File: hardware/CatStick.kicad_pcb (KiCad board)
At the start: 4 copper layers, 81 x 20 mm, 80 parts, among them J1 Antenna, J2 Conn_01x06_Female, J3 Conn_01x06_Female, P1 USB_C_Plug_USB2.0, SW1 SW, U1 AP2112K-3.3, U2 RFSW8006QTR7, U3 ATSAMD21E18A, U4 0900PC15A0036, U5 0900FM15D0039, U6 SW409, U7 SX1262IMLTRT, U8 CC1352R1F3RGZR, Y1 48MHz, Y2 32.768kHz, Y3 32Mhz

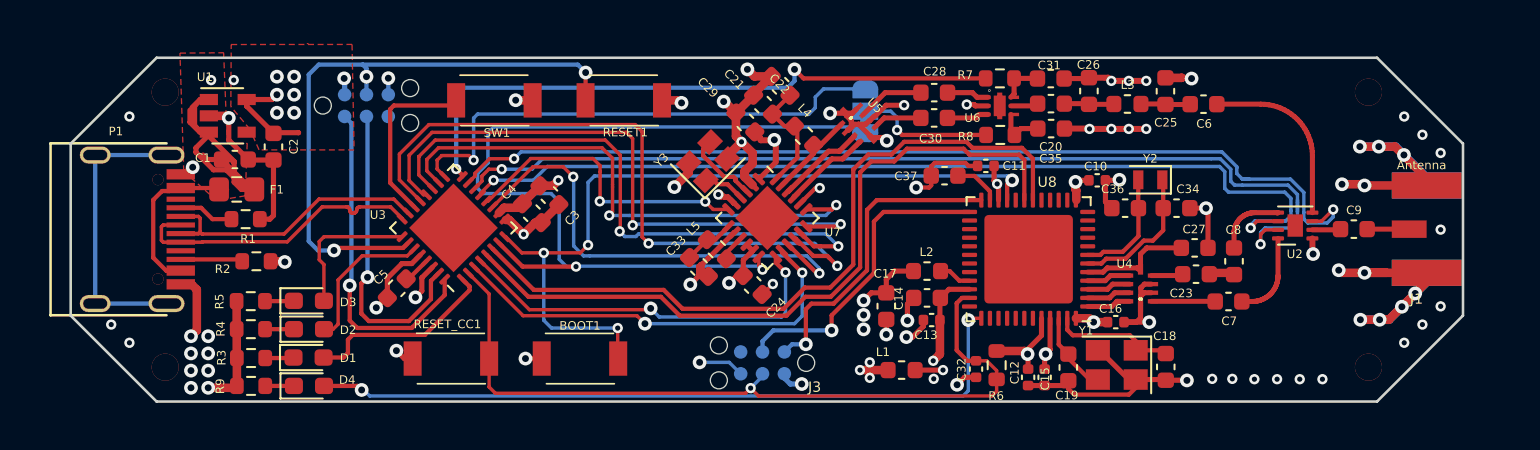
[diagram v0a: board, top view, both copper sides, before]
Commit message: add logos
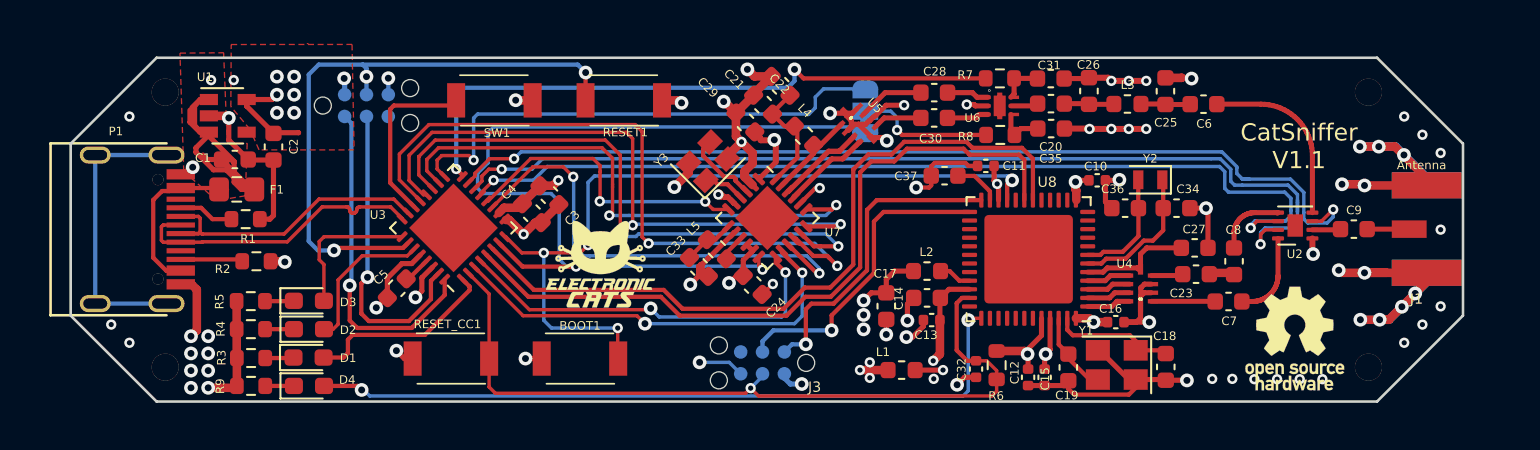
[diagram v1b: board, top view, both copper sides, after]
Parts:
- added G***: LOGO, Aesthetics:electronic_cats_logo_4x3, F.Cu at (115.8, 112.0)
- added G***: LOGO, Aesthetics:electronic_cats_logo_8x6, B.Cu at (110.5, 110.2)
- added REF**: OSHW-Logo_5.7x6mm_SilkScreen, Symbol:OSHW-Logo_5.7x6mm_SilkScreen, F.Cu at (156.2, 116.3)
- added REF**: OSHW-Logo_7.5x8mm_SilkScreen, Symbol:OSHW-Logo_7.5x8mm_SilkScreen, B.Cu at (145.8, 110.7)
- added REF**: ESD-Logo_8.9x8mm_SilkScreen, Symbol:ESD-Logo_8.9x8mm_SilkScreen, B.Cu at (128.5, 110.0)
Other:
- board text added: "CatSniffer V1.1"
- board text added: "CatSniffer v1.1"

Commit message: updatePCB
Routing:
- net +3V3: track 28.6 -> 26.4 mm
- net /VDDS: track 45.1 -> 47.1 mm
- net /VDDR: track 27.8 -> 29.4 mm
- net /cJTAG_TMSC: track 18.4 -> 17.2 mm
- net /DIO3: track 17.6 -> 16.4 mm
- net Net-(JP1-Pad2): track 8.47 -> 7.60 mm
- net /ANT_SW: track 36.9 -> 36.1 mm
- net /BOOT: track 45.5 -> 46.2 mm
- net /cJTAG_TCK: track 18.0 -> 17.4 mm

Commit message: updatePCBvias
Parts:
- moved Y2 3.21 mm to (146.3, 109.9)
- moved C34 2.46 mm to (147.2, 107.5), turned to 90 degrees
- moved C10 1.74 mm to (143.6, 105.8), turned to 90 degrees
- moved C36 1.41 mm to (145.7, 107.5), turned to 90 degrees
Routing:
- net /CTF3: track 54.7 -> 50.3 mm
- net Net-(C36-Pad1): track 6.69 -> 4.32 mm
- net Net-(C34-Pad1): track 8.15 -> 6.01 mm
- net /VDDS: track 47.1 -> 49.1 mm
- net /cJTAG_TMSC: track 17.2 -> 18.6 mm
- net /cJTAG_TCK: track 17.4 -> 18.7 mm
- net GND: track 153.5 -> 152.5 mm, vias 77 -> 78
- net /CIPO: track 40.4 -> 39.3 mm
- net /CTF1: track 56.5 -> 55.5 mm
- net /SWDIO: track 19.7 -> 20.6 mm
- net /LED3: track 11.4 -> 12.2 mm
- net /ANT_SW: track 36.1 -> 36.8 mm
- net /DIO2: track 51.9 -> 51.1 mm
- net /DIO22: track 29.4 -> 28.7 mm
- net /DIO1: track 22.8 -> 22.0 mm
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
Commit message: fixPCBVias
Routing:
- net /NSS: track 31.4 -> 30.8 mm
- net /SCK: track 35.6 -> 35.0 mm

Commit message: fix ground planes
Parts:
- moved C17 0.59 mm to (132.4, 115.0)
- moved C13 0.49 mm to (135.1, 115.8)
- moved C14 0.42 mm to (134.8, 114.4)
- moved L2 0.36 mm to (134.5, 112.6)
- turned C32 to 90 degrees
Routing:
- net /VDDS: track 49.1 -> 65.2 mm
- net GND: track 152.5 -> 166.5 mm
- net +3V3: track 26.1 -> 28.6 mm
- net /VDDR: track 29.0 -> 31.5 mm, vias 5 -> 4
- net /cJTAG_TCK: track 18.7 -> 20.3 mm
- added copper zone on B.Cu, net GND
- added copper zone on F.Cu, net GND

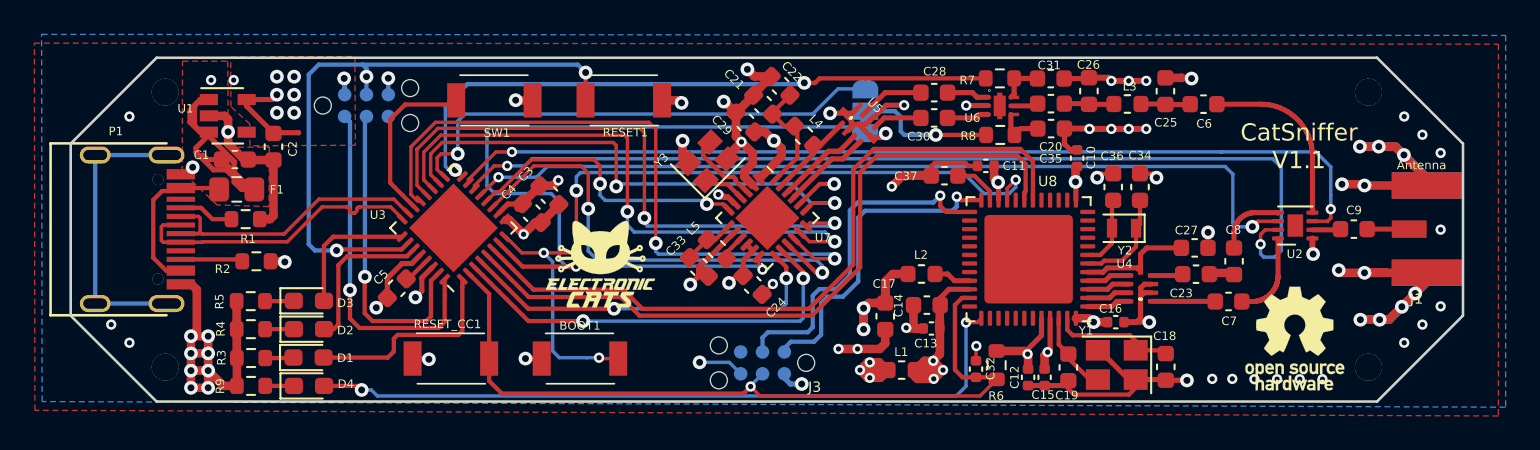
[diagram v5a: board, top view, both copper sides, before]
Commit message: add groudn connection
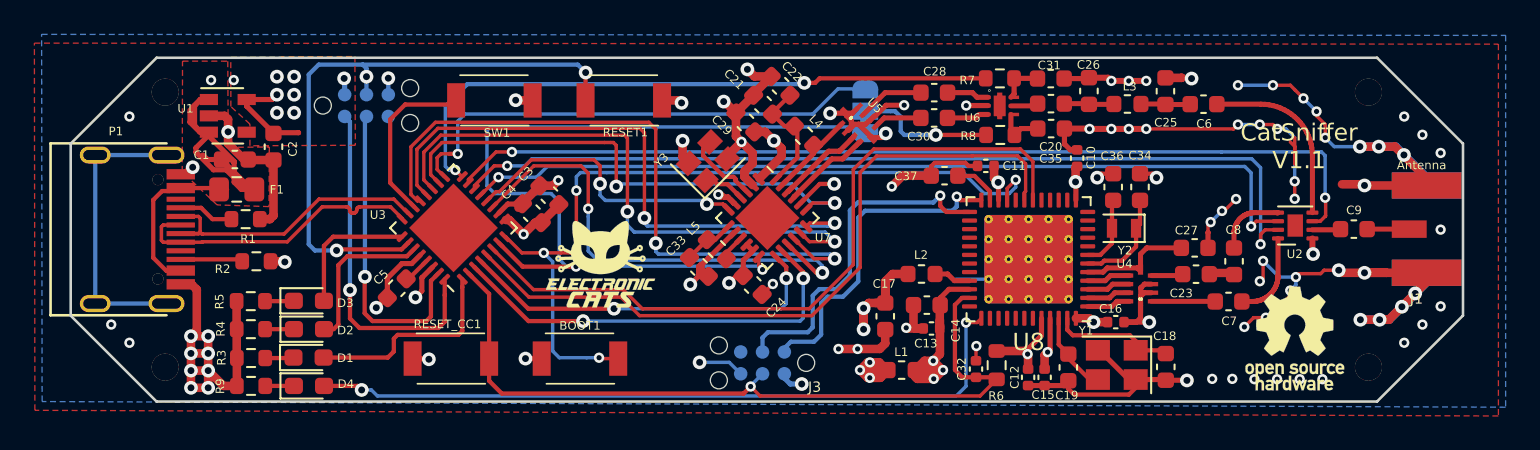
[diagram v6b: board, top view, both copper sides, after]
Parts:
- U8: footprint Package_DFN_QFN:VQFN-48-1EP_7x7mm_P0.5mm_EP5.15x5.15mm -> Package_DFN_QFN:VQFN-48-1EP_7x7mm_P0.5mm_EP5.15x5.15mm_ThermalVias
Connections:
- P1 pad S1: Net-(P1-PadS1) -> GND
- U8 pad 49: (no net) -> GND
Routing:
- net GND: track 166.5 -> 225.5 mm, vias 78 -> 96
- net Net-(P1-PadS1): track 16.9 -> 0.00 mm
- net /CTF2: track 56.5 -> 52.9 mm

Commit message: DRC clean
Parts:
- removed the REF** at (128.5, 110.0)
- moved G*** 20.7 mm to (131.1, 110.5)
- moved G*** 4.27 mm to (117.1, 107.9)
- moved R2 1.15 mm to (94.7, 111.8)
- moved R1 0.52 mm to (94.7, 109.4)
- moved R8 0.05 mm to (139.0, 104.5)
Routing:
- net GND: track 225.5 -> 309.7 mm, vias 96 -> 101
- net /VDDS: track 65.2 -> 58.0 mm
- net VCC: track 21.4 -> 18.2 mm
- net Net-(C35-Pad1): track 2.79 -> 4.70 mm
- net +3V3: track 28.6 -> 29.8 mm
- net Net-(P1-PadB5): track 3.62 -> 2.48 mm
- net /VDDR: track 31.5 -> 30.8 mm
- net Net-(P1-PadA5): track 3.22 -> 2.71 mm
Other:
- board text added: "&"
- board text added: "Paulino Calderon"

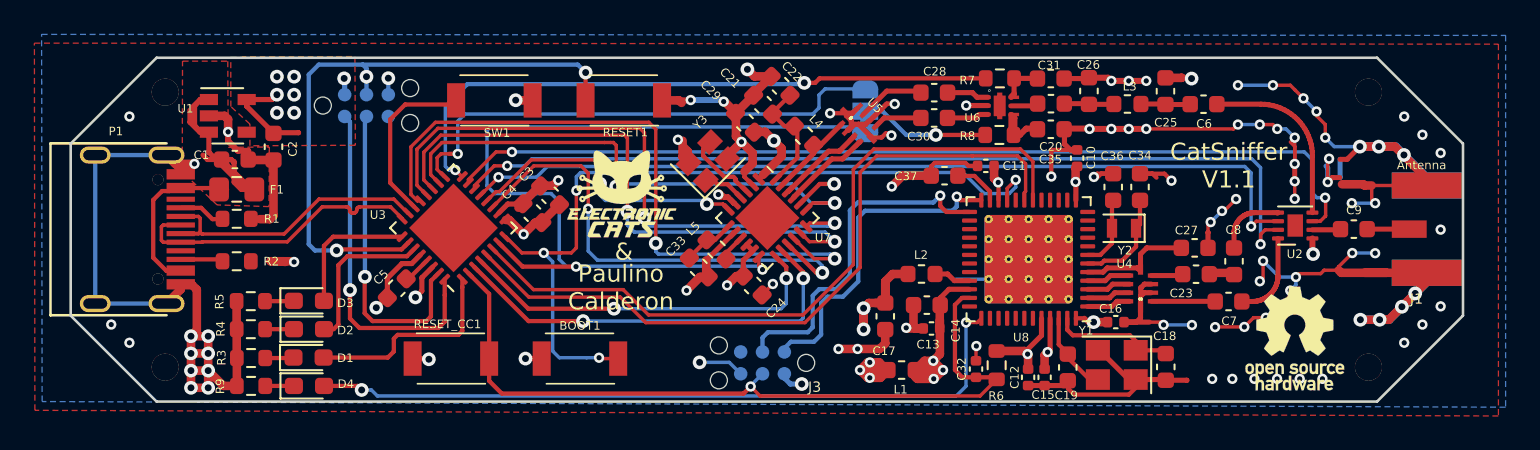
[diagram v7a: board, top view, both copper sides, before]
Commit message: update traces RX/TX
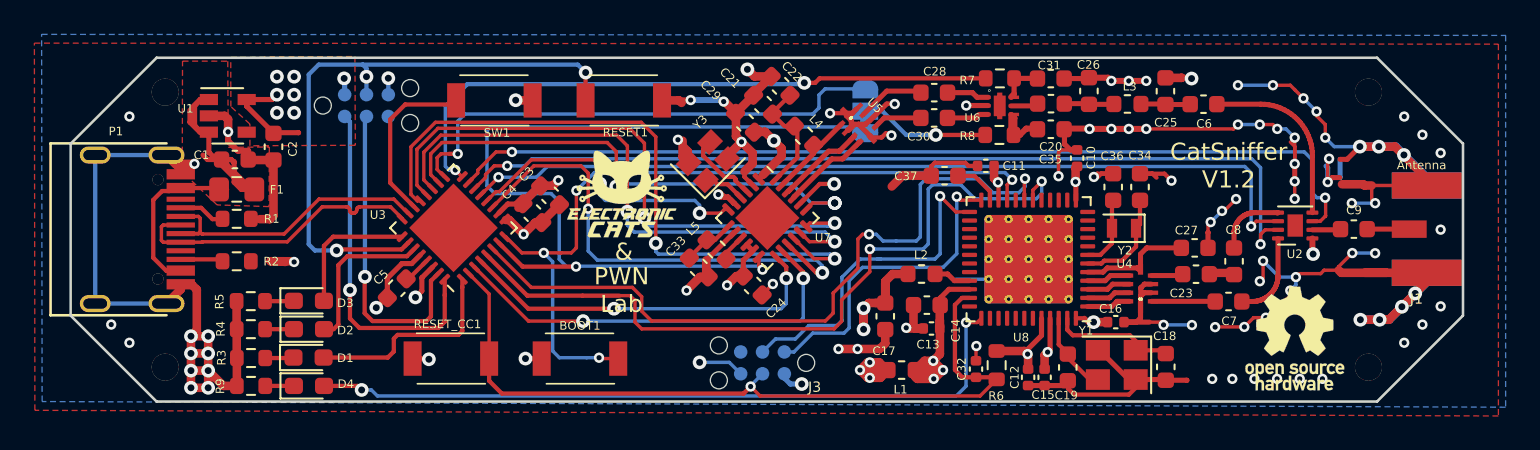
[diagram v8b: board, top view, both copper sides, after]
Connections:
- U8 pad 18: /RXD -> /TXD
- U8 pad 19: /TXD -> /RXD
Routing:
- net /TXD: track 42.6 -> 46.3 mm, vias 0 -> 2
- net /BOOT: track 46.9 -> 45.2 mm
- net /cJTAG_TCK: track 20.3 -> 19.8 mm
- net /NSS: track 30.8 -> 30.6 mm, vias 2 -> 3
- net /RXD: track 42.8 -> 42.6 mm, vias 0 -> 2
- net GND: track 309.7 -> 309.6 mm, vias 101 -> 100
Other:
- board text added: "CatSniffer V1.2"
- board text added: "CatSniffer v1.2"
- board text added: "PWN Lab"
- board text added: "electroniccats.com"
- board text added: "pwnlab.com.mx"
- board text removed: "CatSniffer V1.1"
- board text removed: "CatSniffer v1.1"
- board text removed: "Paulino Calderon"
